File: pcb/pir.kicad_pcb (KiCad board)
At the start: 2 copper layers, 132 parts, among them IC1 MAX44009EDT+T, IC2 IRA-S210ST01, IC3 EL817S, IC4 EL817S, IC5 SI2302CDS-T1-GE3, IC6 SI2302CDS-T1-GE3, J2 FH12-24S-0.5SH(55), J3 SWD, J4 UART, Q1 SI2323DS, SW1 SW_Push, SW2 SW_Push, SW3 SW_Push, SW4 SW_Push, SW5 SW_Push, U1 STM32L476RETx, Y1 32 Mhz, Y2 32 Mhz

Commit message: Reassigned some footprints, added some libraries
Normally I can start working on PCB.
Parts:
- removed IC5, IC6: SI2302CDS-T1-GE3, SI2323DS-T1-E3:SOT95P237X112-3N
- removed TP40, TP41: TEST, Measurement_Points:Measurement_Point_Round-TH_Small
- added C41: 0.1uF, Capacitors_SMD:C_1206, F.Cu at (107.7, 45.3)
- added D2: MBR0530, MBR0530:SOD3716X135N, F.Cu at (63.1, 68.4)
- added D3: MBR0530, MBR0530:SOD3716X135N, F.Cu at (28.1, 37.6)
- added D4: MBR0530, MBR0530:SOD3716X135N, F.Cu at (21.1, 50.3)
- added D5: MBR0530, MBR0530:SOD3716X135N, F.Cu at (28.1, 41.4)
- added D6: MBR0530, MBR0530:SOD3716X135N, F.Cu at (165.5, 24.9)
- added D7: MBR0530, MBR0530:SOD3716X135N, F.Cu at (177.0, 19.7)
- added D8: MBR0530, MBR0530:SOD3716X135N, F.Cu at (159.0, 35.8)
- added IC7: EL817S, EL817S:EL817S, F.Cu at (149.0, 36.5)
- added IC8: EL817S, EL817S:EL817S, F.Cu at (160.6, 31.3)
- added J1: SJ-2523-SMT-TR, SJ-2523-SMT-TR:SJ-2523-SMT-TR, F.Cu at (145.4, 22.7)
- added JP4: Jumper, Pin_Headers:Pin_Header_Straight_1x02_Pitch2.54mm, F.Cu at (87.2, 34.2)
- added Q2: RE1C002UN, RE1C002UNTCL:SOT50P160X85-3N, F.Cu at (22.3, 26.9)
- added Q3: RE1C002UN, RE1C002UNTCL:SOT50P160X85-3N, F.Cu at (44.0, 19.1)
- added R28: 150, Resistors_SMD:R_1206, F.Cu at (168.3, 29.6)
- added R29: 150, Resistors_SMD:R_1206, F.Cu at (174.8, 24.4)
- added R30: 150, Resistors_SMD:R_1206, F.Cu at (168.3, 35.5)
- added R31: 36k, Resistors_SMD:R_1206, F.Cu at (184.3, 26.5)
- added R32: 2.9k, Resistors_SMD:R_1206, F.Cu at (184.0, 20.6)
- added R33: 2.2k, Resistors_SMD:R_1206, F.Cu at (173.0, 30.2)
- added R34: 150, Resistors_SMD:R_1206, F.Cu at (179.5, 26.5)
- C14, C15, C16, C17, C18, C19, C20, C21, C22, C23, C24, C25, C26, C27, C28, C29, C30, C31, C32, C33, C34, C35, C36, C37, C38, C39, C40: footprint Capacitors_SMD:C_1210 -> Capacitors_SMD:C_1206
- J3: footprint Pin_Headers:Pin_Header_Angled_1x06_Pitch2.54mm -> Pin_Headers:Pin_Header_Straight_1x06_Pitch2.54mm
- J4, JP3: footprint Pin_Headers:Pin_Header_Angled_1x03_Pitch2.54mm -> Pin_Headers:Pin_Header_Straight_1x03_Pitch2.54mm
- JP1, JP2: footprint Pin_Headers:Pin_Header_Angled_1x02_Pitch2.54mm -> Pin_Headers:Pin_Header_Straight_1x02_Pitch2.54mm
- R1, R10, R11, R12, R13, R14, R15, R16, R17, R18, R19, R2, R21, R22, R23, R24, R25, R26, R27, R3, R4, R5, R6, R7, R8, R9: footprint Resistors_SMD:R_1210 -> Resistors_SMD:R_1206
- R20: value 1K -> 10k; footprint Resistors_SMD:R_1210 -> Resistors_SMD:R_1206
- moved SW4 259.6 mm to (20.0, 33.3)
- moved SW2 257.0 mm to (20.0, 43.3)
- moved TP17 254.9 mm to (25.5, 31.3)
- moved SW5 249.3 mm to (31.6, 30.6)
- moved R25 248.4 mm to (28.1, 46.1)
- moved TP12 243.8 mm to (34.7, 39.5)
- moved TP21 243.2 mm to (37.1, 33.5)
- moved TP15 242.2 mm to (34.7, 45.6)
- moved SW3 241.4 mm to (41.7, 25.4)
- moved TP11 239.9 mm to (38.8, 39.5)
- moved TP19 239.4 mm to (41.1, 33.5)
- moved R17 238.0 mm to (39.1, 45.4)
- moved TP18 236.9 mm to (47.2, 23.4)
- moved L1 236.8 mm to (38.9, 51.2)
- moved TP13 234.5 mm to (45.2, 36.9)
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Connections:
- IC1 pad 1: VCC -> Net-(C41-Pad1)
- IC3 pad 4: SHIELD -> Net-(D6-Pad2)
- IC4 pad 3: TIP -> Net-(IC4-Pad3)
- IC4 pad 4: SHIELD -> Net-(D7-Pad2)
- U1 pad 44: Net-(TP40-Pad1) -> /camera/PANASHUTTER
- U1 pad 45: /sensor/Ambient -> /camera/PANAFOCUS
- U1 pad 56: Net-(TP41-Pad1) -> /sensor/Ambient

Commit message: Fixed board dimensions
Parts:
- IC2, J1, SW1, SW2, SW3, SW4, SW5: moved to B.Cu
- moved IC4 200.9 mm to (-30.2, -17.8)
- moved C1 199.0 mm to (-81.0, 1.43)
- moved C11 199.0 mm to (-66.5, -4.72)
- moved C15 199.0 mm to (-139.4, 46.3)
- moved C19 199.0 mm to (-136.9, 13.1)
- moved C21 199.0 mm to (-131.9, 7.22)
- moved C29 199.0 mm to (-146.9, 11.7)
- moved C6 199.0 mm to (-82.0, -10.3)
- moved D4 199.0 mm to (-174.5, 13.4)
- moved D7 199.0 mm to (-18.6, -17.2)
- moved IC8 199.0 mm to (-35.0, -5.56)
- moved J4 199.0 mm to (-111.6, 40.2)
- moved JP1 199.0 mm to (-135.3, 23.8)
- moved L1 199.0 mm to (-156.7, 14.4)
- moved Q1 199.0 mm to (-141.8, 32.3)
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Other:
- board outline added: 80 x 100 mm
- rule trace_min: 0.2 -> 0.1

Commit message: Started placing some components, finally
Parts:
- added MK1: IML-0688, Murata-Fresnel:IML-0688, B.Cu at (107.8, 29.4)
- C1, C2, C3, C35, C36, C4, C41, C5, C6, C7, IC1, R1, R2, R3, R4, Y1: moved to B.Cu
- D1: footprint Air_Coils_SML_NEOSID:Neosid_Air-Coil_SML_6-10turn_HDM0431A-HDM1031A -> Diodes_SMD:D_SOD-123
- moved C17 251.9 mm to (117.6, 40.8), turned to 90 degrees
- moved C13 249.8 mm to (106.4, 47.6)
- moved TP10 249.0 mm to (117.6, 45.4)
- moved R11 248.1 mm to (103.8, 53.6)
- moved C15 246.2 mm to (106.8, 40.8), turned to 90 degrees
- moved C16 237.9 mm to (112.2, 40.8), turned to 90 degrees
- moved Q1 237.4 mm to (94.8, 52.0), turned to 180 degrees
- moved JP1 235.5 mm to (97.2, 60.8), turned to 180 degrees
- moved D2 232.9 mm to (99.6, 52.0), turned to 270 degrees
- moved C14 228.0 mm to (101.4, 40.8), turned to 90 degrees
- moved JP2 214.7 mm to (69.8, 60.6), turned to 180 degrees
- moved J3 195.7 mm to (76.6, 60.6), turned to 90 degrees
- moved C6 181.2 mm to (95.4, 27.0), turned to 270 degrees
- moved TP3 170.1 mm to (65.6, 33.4)
- moved IC1 169.0 mm to (59.2, 29.6)
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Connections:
- U1 pad 2: Net-(TP28-Pad1) -> /soc/EINK_PWR
- U1 pad 29: /soc/Down -> /soc/Up
- U1 pad 30: /soc/OK -> /soc/Down
- U1 pad 33: /soc/EINK_D/C -> /soc/OK
- U1 pad 53: Net-(TP35-Pad1) -> /soc/EINK_D/C
- U1 pad 56: /sensor/Ambient -> /soc/EINK_MOSI
- U1 pad 57: /soc/EINK_MOSI -> /sensor/Ambient
- U1 pad 58: /soc/EINK_PWR -> /sensor/SCL
- U1 pad 59: /soc/Left -> /sensor/SDA
- U1 pad 61: /soc/Right -> /soc/Left
- U1 pad 62: /soc/Up -> /soc/Right
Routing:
- net Earth: track 0.00 -> 131.9 mm, vias 0 -> 1
- net VCC: track 0.00 -> 75.0 mm
- net /sensor/SCL: track 0.00 -> 69.1 mm
- net /sensor/Ambient: track 0.00 -> 65.8 mm
- net /sensor/SDA: track 0.00 -> 56.8 mm
- net Net-(D2-Pad2): track 0.00 -> 51.2 mm
- net Net-(C1-Pad1): track 0.00 -> 23.0 mm
- net Net-(BT1-Pad1): track 0.00 -> 17.6 mm
- net Net-(JP3-Pad2): track 0.00 -> 15.6 mm
- net Net-(C41-Pad1): track 0.00 -> 9.71 mm
- net Net-(C37-Pad2): track 0.00 -> 9.29 mm
- net Net-(C39-Pad2): track 0.00 -> 9.03 mm
- net Net-(JP1-Pad2): track 0.00 -> 8.71 mm
- net /battery/Debugger3V3: track 0.00 -> 6.80 mm
- net Net-(C36-Pad2): track 0.00 -> 5.69 mm, vias 0 -> 1
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
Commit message: More work on the PCB
The opamp circuit is done.
Currently working on camera interface.
TODO: screen, buttons.
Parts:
- C10, R6: moved to B.Cu
- C19: value 100n -> 4.7uF
- C31: value 1uF -> 4.7uF
- C35, C36, Y1: moved to F.Cu
- L1: value 68nH -> 68uH
- R17: value 3R -> 0.47
- moved D7 211.4 mm to (123.6, 139.3)
- moved R33 203.4 mm to (123.6, 134.9), turned to 180 degrees
- moved C10 200.2 mm to (117.9, 29.1)
- moved R32 200.2 mm to (123.6, 131.4)
- moved R6 197.7 mm to (117.8, 25.6)
- moved R8 194.5 mm to (68.9, 107.9), turned to 180 degrees
- moved R34 194.4 mm to (123.9, 124.5)
- moved R31 193.5 mm to (123.9, 128.1)
- moved D6 192.5 mm to (90.4, 138.2)
- moved D1 191.6 mm to (57.6, 100.3)
- moved TP8 187.0 mm to (45.8, 110.8), turned to 270 degrees
- moved R10 185.1 mm to (63.4, 100.4)
- moved R9 183.9 mm to (63.4, 104.1), turned to 180 degrees
- moved TP7 183.2 mm to (45.9, 114.2), turned to 270 degrees
- moved IC8 181.4 mm to (114.4, 97.3), turned to 90 degrees
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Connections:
- U1 pad 56: /soc/EINK_MOSI -> /sensor/Ambient
- U1 pad 57: /sensor/Ambient -> /soc/EINK_MOSI
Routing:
- net /sensor/OPAMP1+: track 0.00 -> 169.8 mm
- net Earth: track 131.9 -> 238.6 mm, vias 1 -> 4
- net /soc/EINK_SCK: track 0.00 -> 54.0 mm, vias 0 -> 4
- net /sensor/OPAMP2+: track 0.00 -> 44.9 mm, vias 0 -> 3
- net Net-(TP38-Pad1): track 0.00 -> 39.8 mm, vias 0 -> 1
- net Net-(IC8-Pad1): track 0.00 -> 35.5 mm
- net /sensor/OPAMP2-: track 0.00 -> 32.0 mm, vias 0 -> 1
- net /sensor/OPAMP1OUT: track 0.00 -> 31.4 mm, vias 0 -> 1
- net /sensor/OPAMP1-: track 0.00 -> 31.3 mm
- net VCC: track 75.0 -> 102.2 mm, vias 0 -> 2
- net /sensor/OPAMP2OUT: track 0.00 -> 26.1 mm
- net Net-(IC7-Pad1): track 0.00 -> 25.7 mm
- net /camera/FOCUS: track 0.00 -> 20.5 mm
- net /camera/SHUTTER: track 0.00 -> 19.7 mm
- net Net-(IC4-Pad1): track 0.00 -> 17.3 mm
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
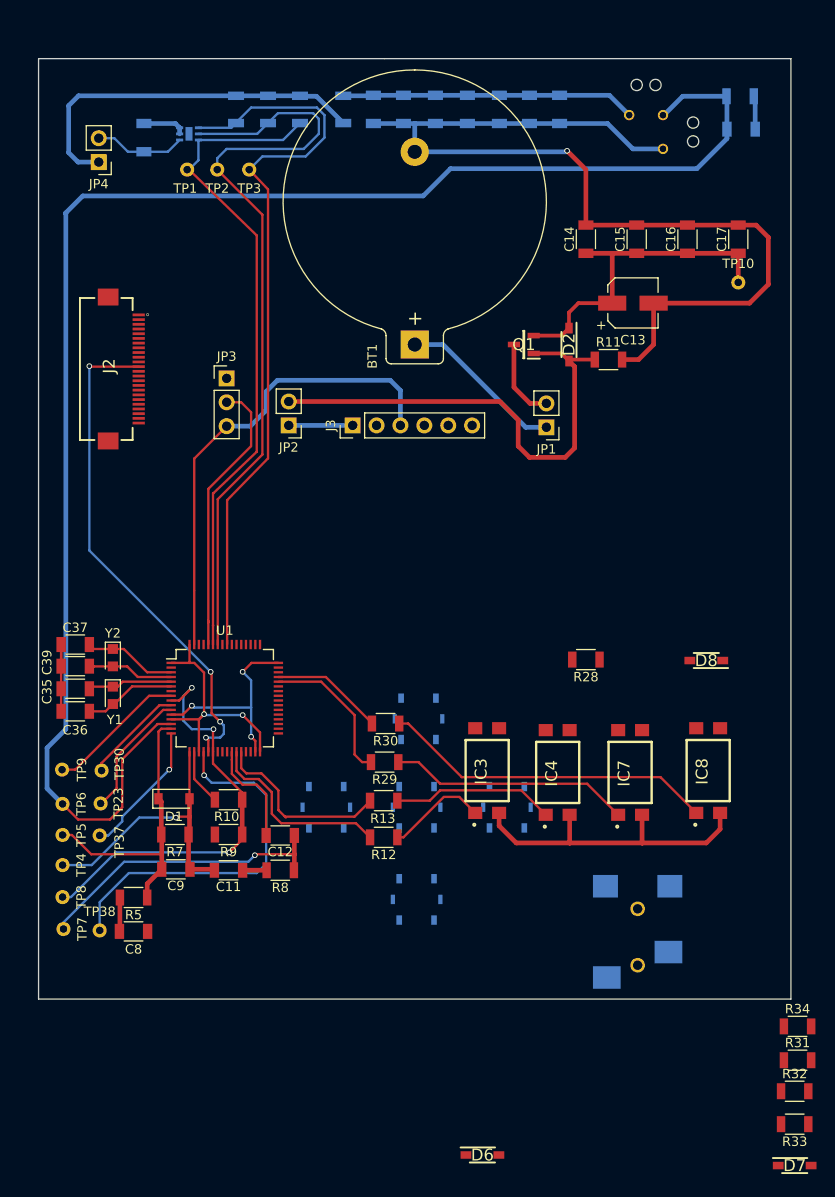
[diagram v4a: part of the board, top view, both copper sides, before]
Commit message: Camera interface placement done.
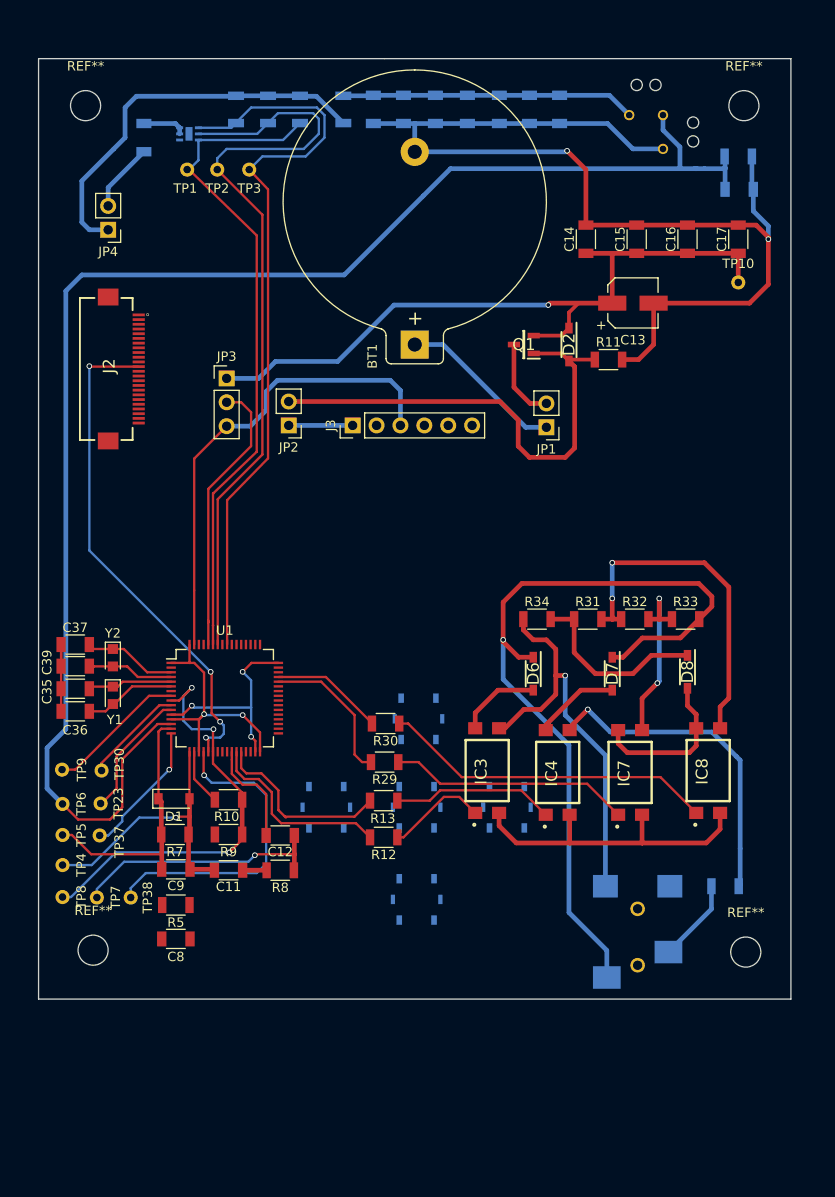
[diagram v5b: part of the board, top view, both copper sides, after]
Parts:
- added REF**: MountingHole_3.2mm_M3, Mounting_Holes:MountingHole_3.2mm_M3, F.Cu at (49.0, 116.4)
- added REF**: MountingHole_3.2mm_M3, Mounting_Holes:MountingHole_3.2mm_M3, F.Cu at (118.4, 116.6)
- added REF**: MountingHole_3.2mm_M3, Mounting_Holes:MountingHole_3.2mm_M3, F.Cu at (118.2, 26.6)
- added REF**: MountingHole_3.2mm_M3, Mounting_Holes:MountingHole_3.2mm_M3, F.Cu at (48.2, 26.6)
- R28: moved to B.Cu
- moved D7 55.8 mm to (104.2, 87.0), turned to 270 degrees
- moved R33 54.9 mm to (112.0, 81.2), turned to 0 degrees
- moved R32 53.0 mm to (106.6, 81.2)
- moved R31 51.9 mm to (101.6, 81.2)
- moved D6 51.5 mm to (95.8, 87.0), turned to 270 degrees
- moved R34 51.4 mm to (96.2, 81.2)
- moved R28 28.3 mm to (116.2, 109.6), turned to 0 degrees
- moved JP4 7.27 mm to (50.6, 39.8)
- moved C10 6.40 mm to (117.7, 35.5)
- moved R6 6.40 mm to (117.6, 32.0)
- moved TP7 4.88 mm to (49.4, 110.8)
- moved TP38 4.81 mm to (53.0, 110.8)
- moved C8 4.57 mm to (57.8, 115.2)
- moved R5 4.57 mm to (57.8, 111.6)
- moved D8 2.33 mm to (112.2, 86.8), turned to 270 degrees
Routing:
- net SHIELD: track 0.00 -> 86.2 mm, vias 0 -> 1
- net VCC: track 102.2 -> 149.2 mm, vias 2 -> 3
- net RING: track 0.00 -> 42.9 mm, vias 0 -> 1
- net Net-(IC8-Pad3): track 0.00 -> 37.4 mm, vias 0 -> 2
- net Net-(IC4-Pad3): track 0.00 -> 34.9 mm, vias 0 -> 1
- net Net-(D8-Pad1): track 0.00 -> 19.8 mm
- net Net-(IC7-Pad3): track 0.00 -> 19.6 mm, vias 0 -> 2
- net Net-(D8-Pad2): track 0.00 -> 16.9 mm
- net Net-(D7-Pad2): track 0.00 -> 9.14 mm
- net TIP: track 0.00 -> 8.90 mm
- net Net-(D6-Pad2): track 0.00 -> 8.80 mm
- net /sensor/OPAMP1+: track 169.8 -> 161.7 mm
- net Earth: track 238.6 -> 245.0 mm, vias 4 -> 5
- net Net-(TP38-Pad1): track 39.8 -> 33.9 mm
- net /sensor/OPAMP2-: track 32.0 -> 27.2 mm
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
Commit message: Finished the display components placement.
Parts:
- C38, C40, R27: moved to B.Cu
- L1: footprint Inductors_SMD:L_0402 -> Inductors_SMD:L_1206
- moved TP18 245.9 mm to (72.8, 94.0)
- moved Q2 242.6 mm to (59.0, 60.0)
- moved D4 241.2 mm to (58.2, 77.0), turned to 180 degrees
- moved D3 241.1 mm to (63.8, 68.8), turned to 270 degrees
- moved D5 235.9 mm to (58.2, 73.2)
- moved Q3 229.6 mm to (54.6, 83.2), turned to 180 degrees
- moved L1 224.8 mm to (58.2, 80.2)
- moved R17 220.8 mm to (57.6, 62.8), turned to 180 degrees
- moved C29 211.8 mm to (57.8, 66.0)
- moved R16 209.9 mm to (57.8, 69.4), turned to 180 degrees
- moved C30 205.3 mm to (60.8, 39.8)
- moved C33 204.2 mm to (60.8, 54.6)
- moved C20 200.4 mm to (63.6, 74.6), turned to 270 degrees
- moved C31 197.3 mm to (60.8, 44.6)
- moved C27 196.3 mm to (60.8, 57.6), turned to 180 degrees
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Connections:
- J4 pad 1: TX -> Earth
- J4 pad 3: Earth -> TX
- U1 pad 29: /soc/Up -> Net-(TP39-Pad1)
- U1 pad 30: /soc/Down -> Net-(TP33-Pad1)
- U1 pad 33: /soc/OK -> Net-(TP26-Pad1)
- U1 pad 37: Net-(TP32-Pad1) -> /soc/Down
- U1 pad 38: Net-(TP25-Pad1) -> /soc/Right
- U1 pad 39: Net-(TP33-Pad1) -> /soc/OK
- U1 pad 40: Net-(TP26-Pad1) -> /soc/Left
- U1 pad 41: Net-(TP39-Pad1) -> /soc/Up
- U1 pad 61: /soc/Left -> Net-(TP25-Pad1)
- U1 pad 62: /soc/Right -> Net-(TP32-Pad1)
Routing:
- net /user/PREVGL: track 0.00 -> 60.0 mm
- net /user/PREVGH: track 0.00 -> 55.9 mm
- net /soc/EINK_RST: track 0.00 -> 51.7 mm, vias 0 -> 2
- net VCC: track 149.2 -> 198.8 mm
- net Earth: track 245.0 -> 294.6 mm, vias 5 -> 6
- net /user/EINK_VCC: track 0.00 -> 49.3 mm, vias 0 -> 2
- net /soc/EINK_BUSY: track 0.00 -> 46.1 mm, vias 0 -> 2
- net /soc/EINK_MOSI: track 0.00 -> 46.1 mm, vias 0 -> 2
- net /soc/EINK_BS: track 0.00 -> 46.0 mm, vias 0 -> 2
- net /soc/EINK_CS: track 0.00 -> 45.3 mm, vias 0 -> 2
- net SWO: track 0.00 -> 44.0 mm
- net /soc/EINK_D/C: track 0.00 -> 39.9 mm, vias 0 -> 2
- net TX: track 0.00 -> 33.3 mm, vias 0 -> 1
- net Net-(C20-Pad2): track 0.00 -> 33.0 mm, vias 0 -> 2
- net RX: track 0.00 -> 30.7 mm, vias 0 -> 1
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
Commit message: Placed all components
Still some routing to do though, and many TP's are not placed.
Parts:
- removed the REF** at (118.4, 116.6)
- removed TP14, TP19, TP20, TP21, TP22, TP28, TP35: TEST, Measurement_Points:Measurement_Point_Round-TH_Small
- C38, R27: moved to F.Cu
- moved TP24 221.9 mm to (-206.6, 45.1)
- moved TP25 221.9 mm to (-215.2, 50.8)
- moved TP26 221.9 mm to (-202.5, 39.0)
- moved TP29 221.9 mm to (-220.4, 56.9)
- moved TP31 221.9 mm to (-224.5, 55.5)
- moved TP32 221.9 mm to (-206.6, 39.0)
- moved TP33 221.9 mm to (-228.5, 55.5)
- moved TP34 221.9 mm to (-211.1, 50.8)
- moved TP36 221.9 mm to (-198.4, 39.0)
- moved TP39 221.9 mm to (-203.0, 51.1)
- moved TP27 221.9 mm to (-216.3, 56.9)
- moved R25 163.9 mm to (89.1, 82.1), turned to 270 degrees
- moved R26 145.8 mm to (87.7, 85.7), turned to 180 degrees
- moved C24 144.6 mm to (80.0, 73.0), turned to 270 degrees
- moved R24 140.1 mm to (87.9, 76.7), turned to 180 degrees
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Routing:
- net Earth: track 294.6 -> 7.75 mm, vias 6 -> 0
- net Net-(C38-Pad2): track 8.57 -> 77.9 mm, vias 1 -> 2
- net SWDIO: track 0.00 -> 43.4 mm, vias 0 -> 1
- net SWCLK: track 0.00 -> 33.8 mm, vias 0 -> 1
- net /soc/Right: track 0.00 -> 30.1 mm, vias 0 -> 2
- net nRESET: track 0.00 -> 26.8 mm
- net /soc/OK: track 0.00 -> 25.5 mm, vias 0 -> 2
- net /soc/Up: track 0.00 -> 24.1 mm, vias 0 -> 2
- net /soc/Down: track 0.00 -> 23.0 mm, vias 0 -> 2
- net /soc/Left: track 0.00 -> 13.7 mm, vias 0 -> 2
- net /user/EINK_VCC: track 49.3 -> 60.0 mm, vias 2 -> 3
- net /soc/EINK_PWR: track 4.06 -> 12.1 mm
- net /sensor/OPAMP2+: track 44.9 -> 41.4 mm
- net Net-(R18-Pad2): track 0.00 -> 2.63 mm
- net Net-(R23-Pad2): track 0.00 -> 2.41 mm
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- added copper zone on B.Cu, net Earth
- added copper zone on F.Cu, net Earth

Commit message: Very few routes remaining
Many TP's will be removed due to lack of space.
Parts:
- moved TP18 258.8 mm to (-182.9, 54.0)
- moved R10 0.91 mm to (63.3, 101.3)
- moved SW4 0.72 mm to (73.2, 101.6)
- moved SW5 0.63 mm to (83.2, 111.6)
- moved SW1 0.45 mm to (93.2, 101.6)
- moved SW3 0.45 mm to (83.2, 101.6)
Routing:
- net VCC: track 198.8 -> 332.6 mm, vias 3 -> 4
- net Net-(R14-Pad2): track 2.17 -> 73.3 mm, vias 0 -> 1
- net Net-(R18-Pad2): track 2.63 -> 39.5 mm, vias 0 -> 1
- net Net-(R23-Pad2): track 2.41 -> 38.2 mm, vias 0 -> 1
- net Net-(R25-Pad2): track 2.17 -> 36.5 mm, vias 0 -> 1
- net Net-(R21-Pad2): track 2.41 -> 30.3 mm, vias 0 -> 1
- net /sensor/OPAMP2OUT: track 26.1 -> 53.9 mm, vias 0 -> 1
- net /sensor/OPAMP2-: track 27.2 -> 41.1 mm, vias 1 -> 2
- net Earth: track 7.75 -> 18.7 mm, vias 0 -> 5
- net /sensor/OPAMP1-: track 27.7 -> 33.9 mm
- net /sensor/OPAMP2+: track 41.4 -> 38.6 mm
